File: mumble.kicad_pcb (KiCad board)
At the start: 2 copper layers, 100 x 30 mm, 61 parts, among them J1 Serial, J10 M1, J101 USB_B_Micro, J11 X_MOT, J12 M0, J13 M1, J16 Z_MOT, J2 Servo, J3 VM sel, J6 Limit Switches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

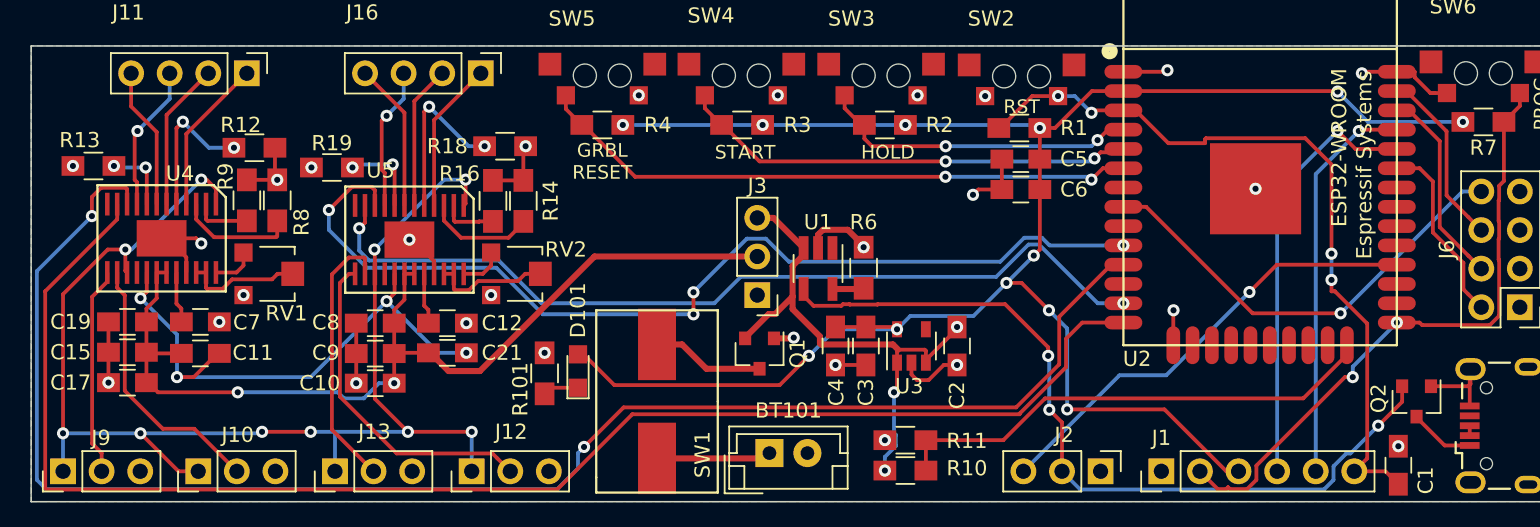
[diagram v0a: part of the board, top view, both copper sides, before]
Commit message: Updated caps and sense resistors
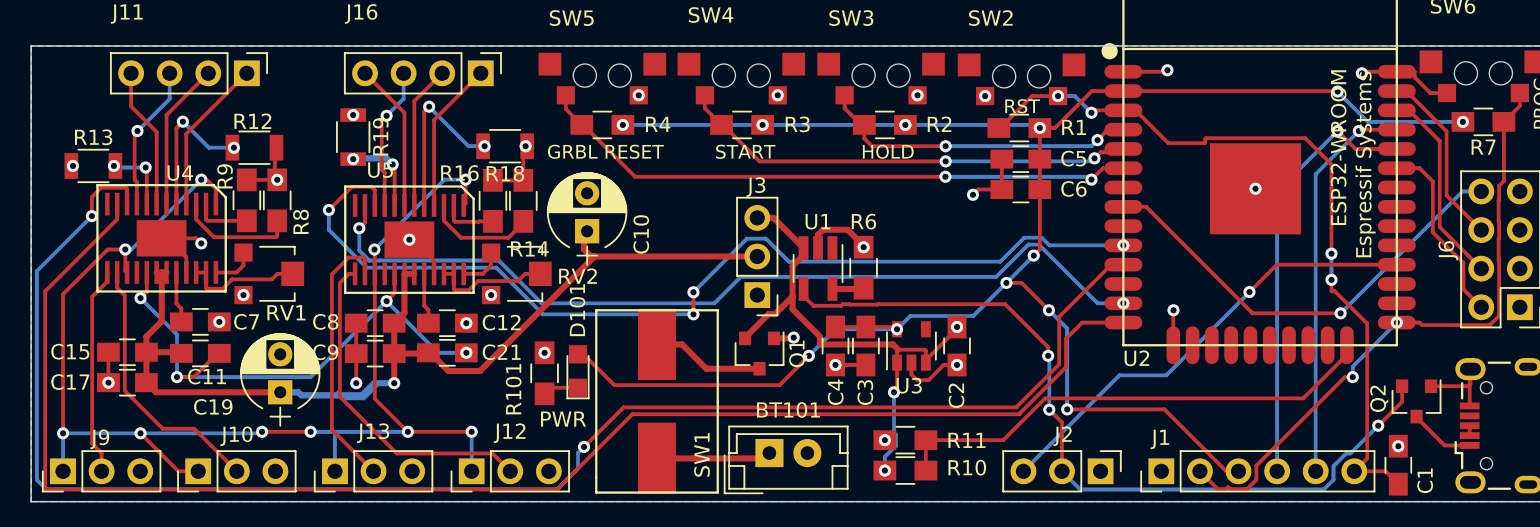
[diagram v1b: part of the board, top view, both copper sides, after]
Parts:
- C10, C19: footprint Capacitors_SMD:C_0805_HandSoldering -> Capacitors_THT:CP_Radial_D5.0mm_P2.50mm
- R101: value R -> 330
- R12, R13, R18, R19: footprint Resistors_SMD:R_0805_HandSoldering -> Resistors_SMD:R_1206
- moved C10 17.2 mm to (121.6, 147.2), turned to 90 degrees
- moved C19 11.1 mm to (101.4, 157.8), turned to 90 degrees
- moved R19 2.44 mm to (106.2, 141.0), turned to 270 degrees
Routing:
- net /VM: track 63.3 -> 76.7 mm, vias 2 -> 1
- net GND: track 59.4 -> 57.4 mm
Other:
- board text added: "MINIGRAPH V1.0"
- board text added: "PWR"

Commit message: Updated some of the errata
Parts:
- added D102: LED, LEDs:LED_0805, F.Cu at (166.4, 157.2)
- added R102: 330, Resistors_SMD:R_0805_HandSoldering, F.Cu at (161.6, 157.2)
- moved R4 17.0 mm to (139.6, 140.4)
- moved SW5 17.0 mm to (139.6, 137.2)
- moved R3 10.5 mm to (121.3, 140.4)
- moved R2 10.5 mm to (130.7, 140.4)
- moved SW3 10.5 mm to (130.4, 137.2)
- moved SW4 10.5 mm to (121.2, 137.2)
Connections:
- J1 pad 2: /PROGRAM -> /RESET
- J1 pad 6: /RESET -> /PROGRAM
- J2 pad 2: VCC -> +BATT
- U2 pad 23: (no net) -> /GPIO15
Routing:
- net /GRBL_RESET: track 39.8 -> 23.3 mm
- net +BATT: track 35.1 -> 47.7 mm
- net /RESET: track 50.1 -> 62.3 mm
- net /START: track 30.2 -> 41.2 mm
- net /HOLD: track 21.2 -> 31.1 mm
- net /PROGRAM: track 41.4 -> 33.4 mm
- net GND: track 57.4 -> 65.2 mm
- net /GPIO15: track 0.00 -> 4.37 mm
- net +3V3: track 127.9 -> 130.3 mm, vias 12 -> 11
- net Net-(D102-Pad1): track 0.00 -> 2.34 mm
- net VCC: track 53.5 -> 55.8 mm, vias 3 -> 2

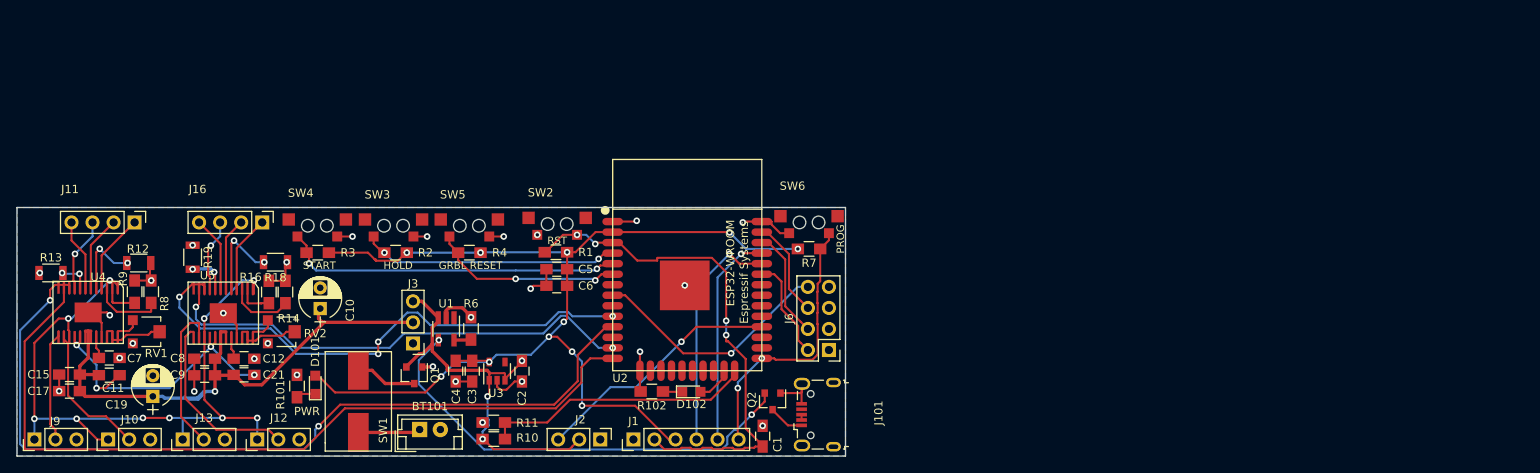
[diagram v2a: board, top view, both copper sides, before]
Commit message: Updated power button and USB connector
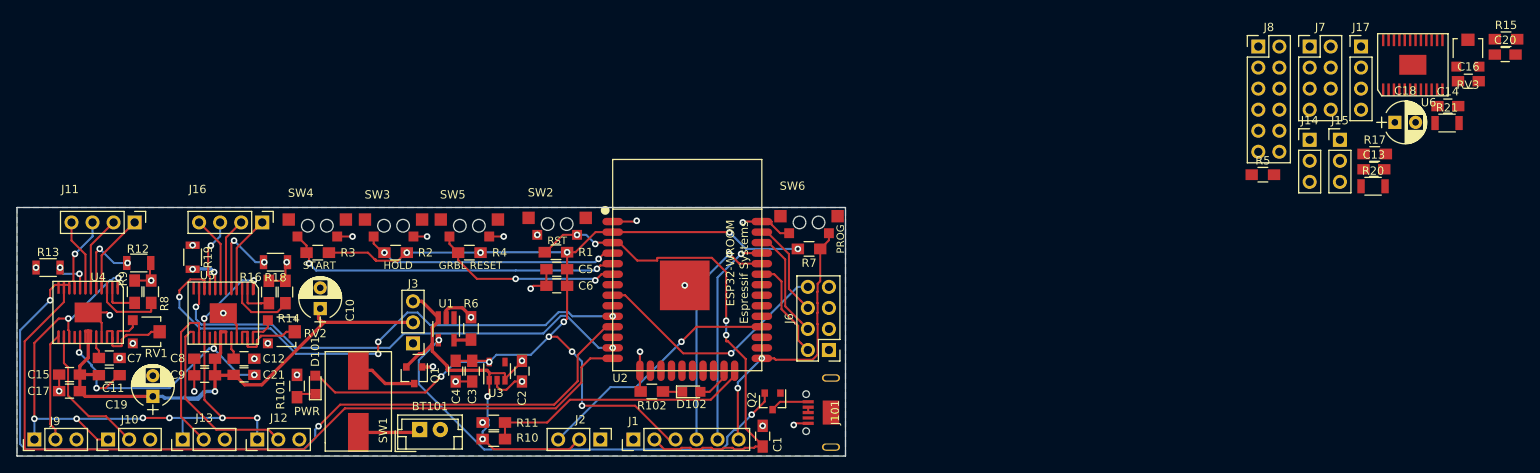
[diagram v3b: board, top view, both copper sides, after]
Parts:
- added C13: 4.7uF, Capacitors_SMD:C_0805_HandSoldering, F.Cu at (248.8, 130.4)
- added C14: 10uF, Capacitors_SMD:C_0805_HandSoldering, F.Cu at (257.7, 122.8)
- added C16: 2.2uF, Capacitors_SMD:C_0805_HandSoldering, F.Cu at (260.2, 119.8)
- added C18: 100uF, Capacitors_THT:CP_Radial_D5.0mm_P2.50mm, F.Cu at (251.3, 124.7)
- added C20: 0.01uF, Capacitors_SMD:C_0805_HandSoldering, F.Cu at (264.6, 116.5)
- added J14: M0, Pin_Headers:Pin_Header_Straight_1x03_Pitch2.54mm, F.Cu at (241.0, 126.8)
- added J15: M1, Pin_Headers:Pin_Header_Straight_1x03_Pitch2.54mm, F.Cu at (244.7, 126.8)
- added J17: Y_MOT, Pin_Headers:Pin_Header_Straight_1x04_Pitch2.54mm, F.Cu at (247.2, 115.6)
- added J7: Front Panel, Pin_Headers:Pin_Header_Straight_2x04_Pitch2.54mm, F.Cu at (241.0, 115.6)
- added J8: Machine Functions, Pin_Headers:Pin_Header_Straight_2x06_Pitch2.54mm, F.Cu at (234.8, 115.6)
- added R15: 47k, Resistors_SMD:R_0805_HandSoldering, F.Cu at (264.7, 114.7)
- added R17: 47k, Resistors_SMD:R_0805_HandSoldering, F.Cu at (248.9, 128.5)
- added R20: 0.1R, Resistors_SMD:R_1206, F.Cu at (248.7, 132.4)
- added R21: 0.1R, Resistors_SMD:R_1206, F.Cu at (257.6, 124.8)
- added R5: 10k, Resistors_SMD:R_0805_HandSoldering, F.Cu at (235.4, 131.0)
- added RV3: 10k, Potentiometers:Potentiometer_Trimmer-EVM3E, F.Cu at (260.1, 116.4)
- added U6: DRV8834, Accelerando:HTSSOP-24, F.Cu at (253.5, 117.8)
- J101: footprint Connectors_USB:USB_Micro-B_Wuerth-629105150521 -> Accelerando:USB_Micro
- moved J101 1.67 mm to (183.2, 159.8)
- moved R13 0.74 mm to (88.8, 142.2)
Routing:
- net GND: track 65.2 -> 60.9 mm, vias 28 -> 29
- net Net-(RV1-Pad2): track 7.80 -> 9.70 mm
- net Net-(RV2-Pad2): track 7.82 -> 9.72 mm
- net /Y_DIR: track 65.3 -> 67.0 mm
- net /VINT: track 87.2 -> 88.4 mm
- net Net-(R13-Pad2): track 4.57 -> 5.47 mm
- net /VCP: track 36.0 -> 36.8 mm

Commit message: Actually saved the PCB this time
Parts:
- removed C13: 4.7uF, Capacitors_SMD:C_0805_HandSoldering
- removed C14: 10uF, Capacitors_SMD:C_0805_HandSoldering
- removed C16: 2.2uF, Capacitors_SMD:C_0805_HandSoldering
- removed C18: 100uF, Capacitors_THT:CP_Radial_D5.0mm_P2.50mm
- removed C20: 0.01uF, Capacitors_SMD:C_0805_HandSoldering
- removed J14: M0, Pin_Headers:Pin_Header_Straight_1x03_Pitch2.54mm
- removed J15: M1, Pin_Headers:Pin_Header_Straight_1x03_Pitch2.54mm
- removed J17: Y_MOT, Pin_Headers:Pin_Header_Straight_1x04_Pitch2.54mm
- removed J7: Front Panel, Pin_Headers:Pin_Header_Straight_2x04_Pitch2.54mm
- removed J8: Machine Functions, Pin_Headers:Pin_Header_Straight_2x06_Pitch2.54mm
- removed R15, R17: 47k, Resistors_SMD:R_0805_HandSoldering
- removed R20, R21: 0.1R, Resistors_SMD:R_1206
- removed R5: 10k, Resistors_SMD:R_0805_HandSoldering
- removed RV3: 10k, Potentiometers:Potentiometer_Trimmer-EVM3E
- removed SW1: SW_SPST, Accelerando:TorchButton
- removed U6: DRV8834, Accelerando:HTSSOP-24
- added POWER: SW_SPST, Accelerando:CherryPowerSwitch, F.Cu at (129.2, 162.0)
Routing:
- net Net-(BT101-Pad1): track 7.54 -> 14.3 mm
- net GND: track 60.9 -> 65.4 mm, vias 29 -> 30
- net Net-(Q1-Pad3): track 7.41 -> 9.80 mm

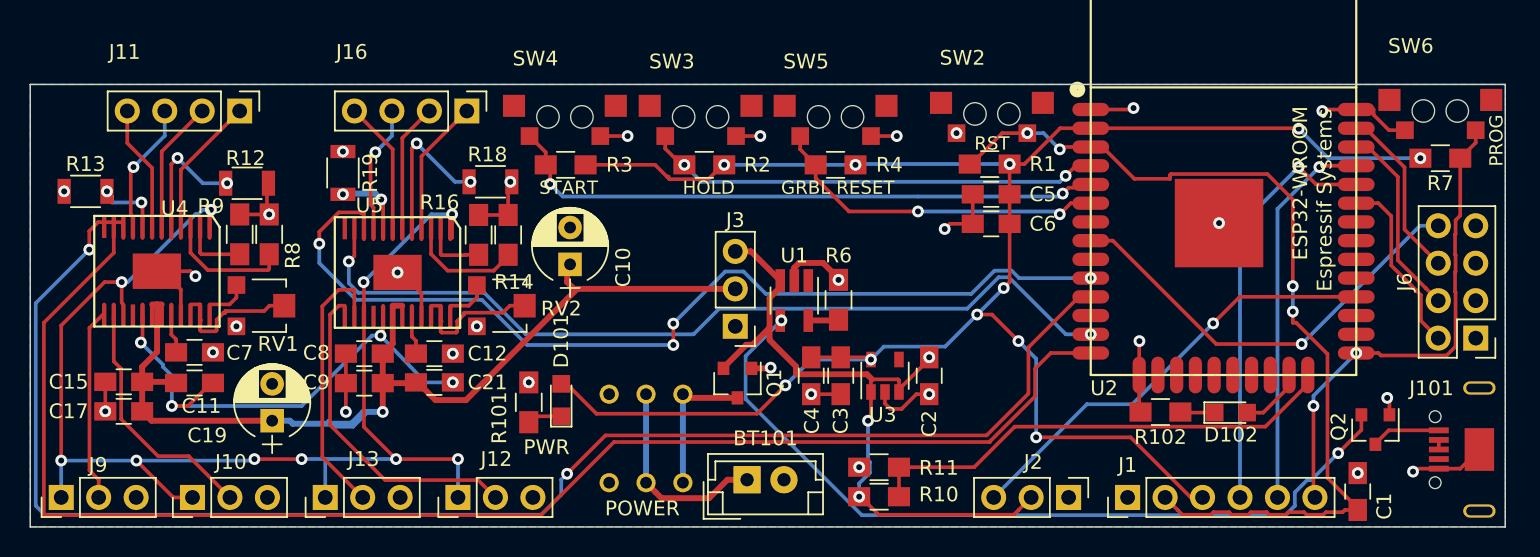
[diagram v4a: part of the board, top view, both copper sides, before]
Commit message: Updated to V1.2 of PCB
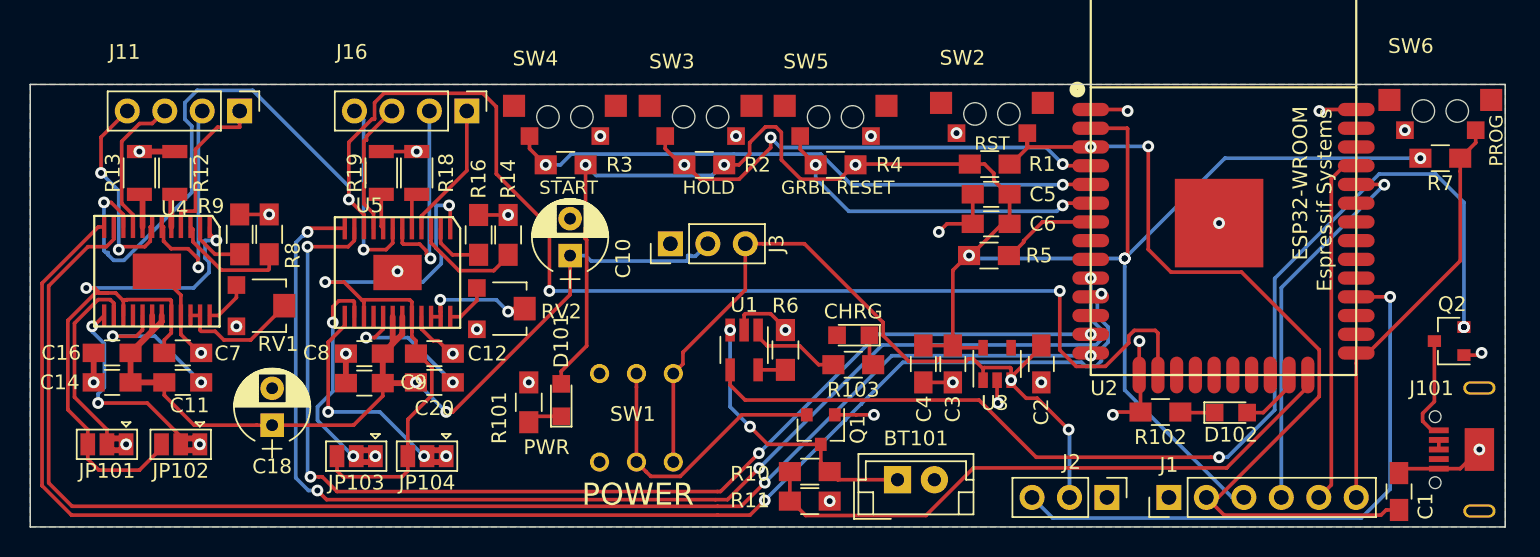
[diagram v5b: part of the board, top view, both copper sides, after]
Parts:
- removed C15: 10uF, Capacitors_SMD:C_0805_HandSoldering
- removed C17: 2.2uF, Capacitors_SMD:C_0805_HandSoldering
- removed C19: 100uF, Capacitors_THT:CP_Radial_D5.0mm_P2.50mm
- removed C21: 0.01uF, Capacitors_SMD:C_0805_HandSoldering
- removed J10, J13: M1, Pin_Headers:Pin_Header_Straight_1x03_Pitch2.54mm
- removed J12, J9: M0, Pin_Headers:Pin_Header_Straight_1x03_Pitch2.54mm
- removed J6: Limit Switches, Pin_Headers:Pin_Header_Straight_2x04_Pitch2.54mm
- removed POWER: SW_SPST, Accelerando:CherryPowerSwitch
- added C14: 10uF, Capacitors_SMD:C_0805_HandSoldering, F.Cu at (90.5, 155.2)
- added C16: 2.2uF, Capacitors_SMD:C_0805_HandSoldering, F.Cu at (90.5, 153.2)
- added C18: 100uF, Capacitors_THT:CP_Radial_D5.0mm_P2.50mm, F.Cu at (101.4, 158.1)
- added C20: 0.01uF, Capacitors_SMD:C_0805_HandSoldering, F.Cu at (112.4, 155.2)
- added CHRG: CHRG, LEDs:LED_0805, F.Cu at (140.8, 152.0)
- added JP101: Jumper_3_Bridged12, Jumper:SolderJumper-3_P1.3mm_Bridged2Bar12_Pad1.0x1.5mm, F.Cu at (90.2, 159.4)
- added JP102: Jumper_3_Bridged12, Jumper:SolderJumper-3_P1.3mm_Bridged2Bar12_Pad1.0x1.5mm, F.Cu at (95.2, 159.4)
- added JP103: Jumper_3_Bridged12, Jumper:SolderJumper-3_P1.3mm_Bridged2Bar12_Pad1.0x1.5mm, F.Cu at (107.1, 160.2)
- added JP104: Jumper_3_Bridged12, Jumper:SolderJumper-3_P1.3mm_Bridged2Bar12_Pad1.0x1.5mm, F.Cu at (111.9, 160.2)
- added R103: 330, Resistors_SMD:R_0805_HandSoldering, F.Cu at (140.8, 154.0)
- added R5: 10k, Resistors_SMD:R_0805_HandSoldering, F.Cu at (150.0, 146.6)
- added SW1: SW_SPST, Accelerando:CherryPowerSwitch, F.Cu at (128.6, 160.6)
- moved BT101 10.2 mm to (143.8, 161.8)
- moved Q2 7.81 mm to (181.2, 152.4), turned to 180 degrees
- moved C2 7.64 mm to (153.6, 153.9)
- moved C3 7.64 mm to (147.6, 153.9)
- moved C4 7.64 mm to (145.6, 153.9)
- moved U3 7.64 mm to (150.6, 153.9)
- moved J3 7.12 mm to (128.4, 145.8), turned to 90 degrees
- moved Q1 6.47 mm to (138.6, 158.4)
- moved R11 5.23 mm to (137.8, 163.2), turned to 0 degrees
- moved R18 5.04 mm to (111.2, 141.0), turned to 270 degrees
- moved R10 5.00 mm to (137.8, 161.2), turned to 180 degrees
- moved R6 4.95 mm to (136.2, 153.0)
- moved R12 4.95 mm to (94.8, 141.0), turned to 270 degrees
- moved U1 4.77 mm to (133.4, 153.0)
- moved R13 3.86 mm to (92.4, 141.0), turned to 270 degrees
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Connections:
- net VCC renamed Net-(Q2-Pad2)
- BT101 pad 1: Net-(BT101-Pad1) -> +BATT
- C11 pad 1: /VCP -> /VCP_X
- C12 pad 1: Net-(C12-Pad1) -> /VINT_Y
- C2 pad 1: +BATT -> /BATT_SWITCHED
- C7 pad 1: Net-(C7-Pad1) -> /VINT_X
- J2 pad 2: +BATT -> /BATT_SWITCHED
- J3 pad 3: +BATT -> /BATT_SWITCHED
- Q1 pad 2: +BATT -> Net-(Q1-Pad2)
- Q1 pad 3: Net-(Q1-Pad3) -> +BATT
- U1 pad 1: (no net) -> /CHRG_ST
- U2 pad 12: /Z_STEP -> (no net)
- U2 pad 16: (no net) -> /STEP_EN
- U2 pad 26: /SPINDLE_SENS -> (no net)
- U2 pad 27: /SPINDLE_ENABLE -> (no net)
- U2 pad 29: /SPINDLE_DIR -> (no net)
- U2 pad 30: /FLOOD -> (no net)
- U2 pad 31: /MIST -> (no net)
- U2 pad 33: /X_LIMIT -> (no net)
- U2 pad 36: /Y_LIMIT -> (no net)
- U2 pad 37: /Z_LIMIT -> (no net)
- U2 pad 8: /PROBE -> (no net)
- U2 pad 9: /Z_DIR -> (no net)
- U3 pad 1: +BATT -> /BATT_SWITCHED
- U3 pad 3: +BATT -> /BATT_SWITCHED
- U4 pad 1: /VINT -> /VINT_X
- U4 pad 10: /X_DIR -> /STEP_EN
- U4 pad 12: (no net) -> /X_DIR
- U4 pad 15: /VINT -> /VINT_X
- U4 pad 17: /VCP -> /VCP_X
- U4 pad 20: Net-(C7-Pad1) -> /VINT_X
- U5 pad 1: /VINT -> /VINT_Y
- U5 pad 10: /Y_DIR -> /STEP_EN
- U5 pad 12: (no net) -> /Y_DIR
- U5 pad 15: /VINT -> /VINT_Y
- U5 pad 17: /VCP -> /VCP_Y
- U5 pad 20: Net-(C12-Pad1) -> /VINT_Y
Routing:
- net /STEP_EN: track 0.00 -> 117.9 mm, vias 0 -> 4
- net /VINT: track 88.4 -> 0.00 mm, vias 10 -> 0
- net /BATT_SWITCHED: track 0.00 -> 54.1 mm, vias 0 -> 2
- net /VINT_X: track 0.00 -> 43.4 mm, vias 0 -> 2
- net /VINT_Y: track 0.00 -> 41.5 mm, vias 0 -> 2
- net /VCP: track 36.8 -> 0.00 mm, vias 4 -> 0
- net /PROBE: track 30.0 -> 0.00 mm, vias 1 -> 0
- net +BATT: track 47.7 -> 19.3 mm, vias 3 -> 2
- net Net-(Q1-Pad2): track 0.00 -> 19.7 mm
- net Net-(Q2-Pad2): track 55.8 -> 75.4 mm, vias 2 -> 3
- net /Y_STEP: track 58.1 -> 77.6 mm, vias 2 -> 4
- net /Y_DIR: track 67.0 -> 83.9 mm
- net Net-(BT101-Pad1): track 14.3 -> 0.00 mm
- net /Y_LIMIT: track 13.2 -> 0.00 mm
- net /X_LIMIT: track 12.5 -> 0.00 mm
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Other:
- board text added: "POWER"
